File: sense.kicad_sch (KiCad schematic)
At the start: 35 parts, among them J6 Rudder, J7 End Stops, J8 Conn_01x02, J9 ISP, U4 AMS1117-5.0, U6 LM317, U7 ATmega328P-AU, Y1 8mhz

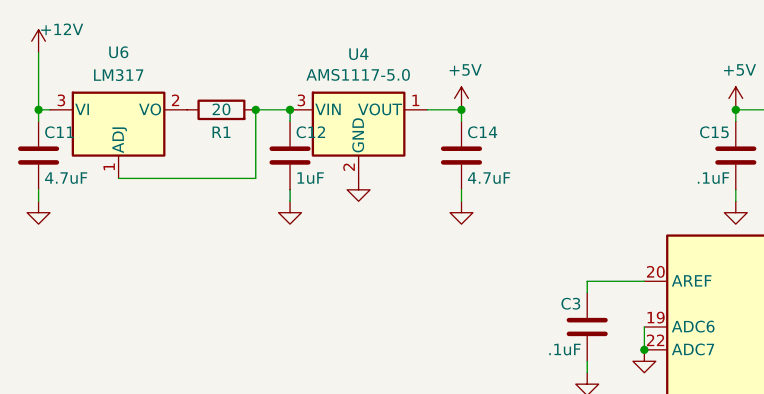
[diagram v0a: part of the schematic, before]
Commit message: Switch from using AMS1117-5.0 to XC6202P502FR-G 5V 200mA LDO regulator
This is what's in the CSV file as the regulator that's being used
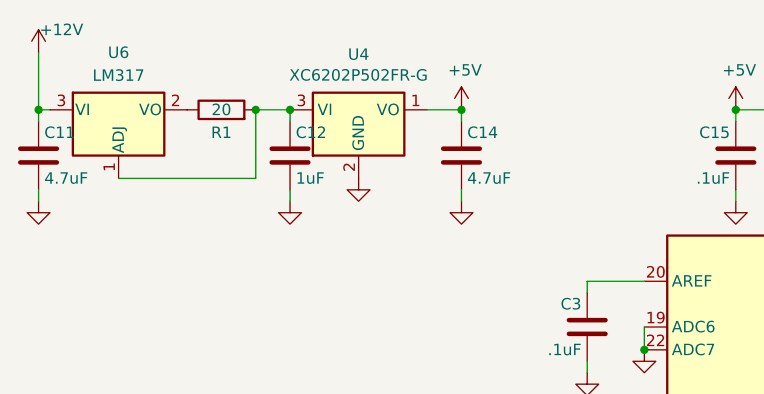
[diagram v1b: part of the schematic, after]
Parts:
- U4: value AMS1117-5.0 -> XC6202P502FR-G; symbol Regulator_Linear:AP2204RB-5.0 -> pypilot_components:XC6202P502FR-G
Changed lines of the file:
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@@
 	)
 	(symbol
-		(lib_id "Regulator_Linear:AP2204RB-5.0")
+		(lib_id "pypilot_components:XC6202P502FR-G")
 		(at 73.66 31.75 0)
 		(unit 1)
@@
 			)
 		)
-		(property "Value" "AMS1117-5.0"
+		(property "Value" "XC6202P502FR-G"
 			(at 73.66 27.9146 0)
 			(effects
@@
 			)
 		)
-		(property "Datasheet" "C513030"
+		(property "Datasheet" "https://www.lcsc.com/datasheet/lcsc_datasheet_2008192005_Torex-Semicon-XC6202P502FR-G_C725695.pdf"
 			(at 76.2 38.1 0)
 			(effects
@@
 			)
 		)
-		(property "Description" ""
+		(property "Description" "200mA Low Dropout regulator, positive, 5.0V fixed output, SOT-223, low power version of AMS1777-5.0"
 			(at 73.66 31.75 0)
 			(effects

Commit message: Remove whitespace from LCSC field entries
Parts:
- C11, C14: LCSC C29823 -> C29823
- LED4: LCSC C2296 -> C2296
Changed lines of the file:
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@@
 			)
 		)
-		(property "LCSC" " C29823"
+		(property "LCSC" "C29823"
 			(at 85.09 36.83 0)
 			(effects
@@
 			)
 		)
-		(property "LCSC" " C29823"
+		(property "LCSC" "C29823"
 			(at 38.1 36.83 0)
 			(effects
@@
 			)
 		)
-		(property "LCSC" " C2296"
+		(property "LCSC" "C2296"
 			(at 97.79 78.74 90)
 			(effects

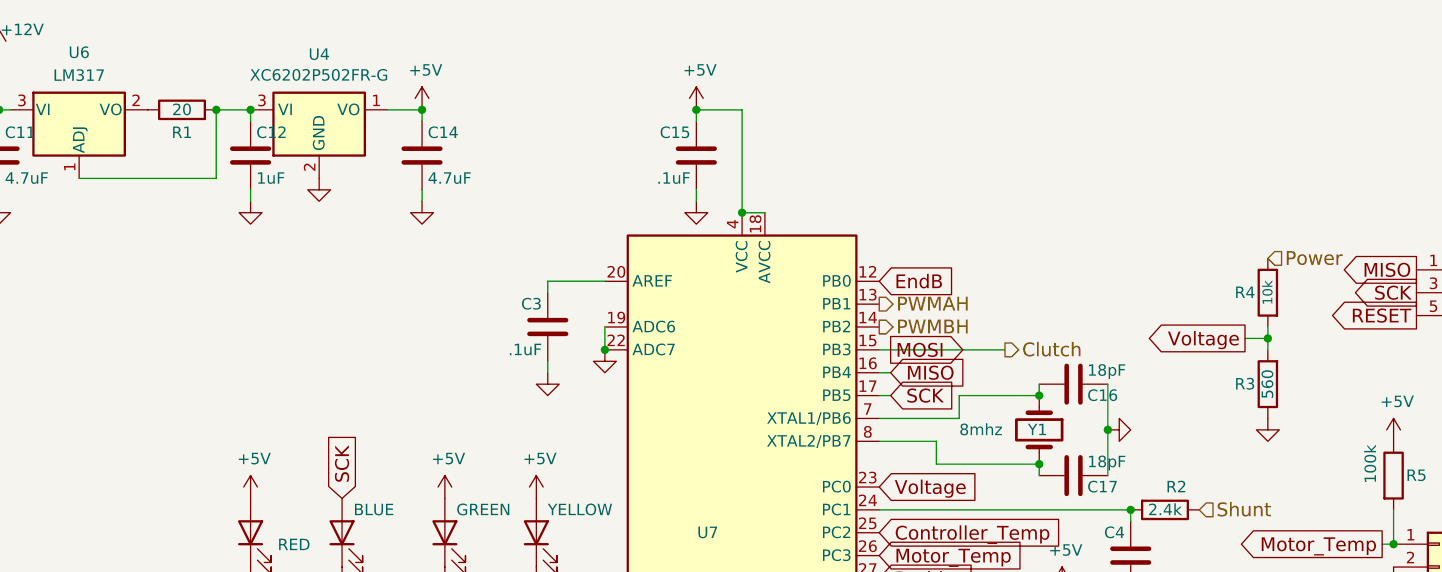
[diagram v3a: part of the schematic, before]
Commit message: Use standard format for resistor values
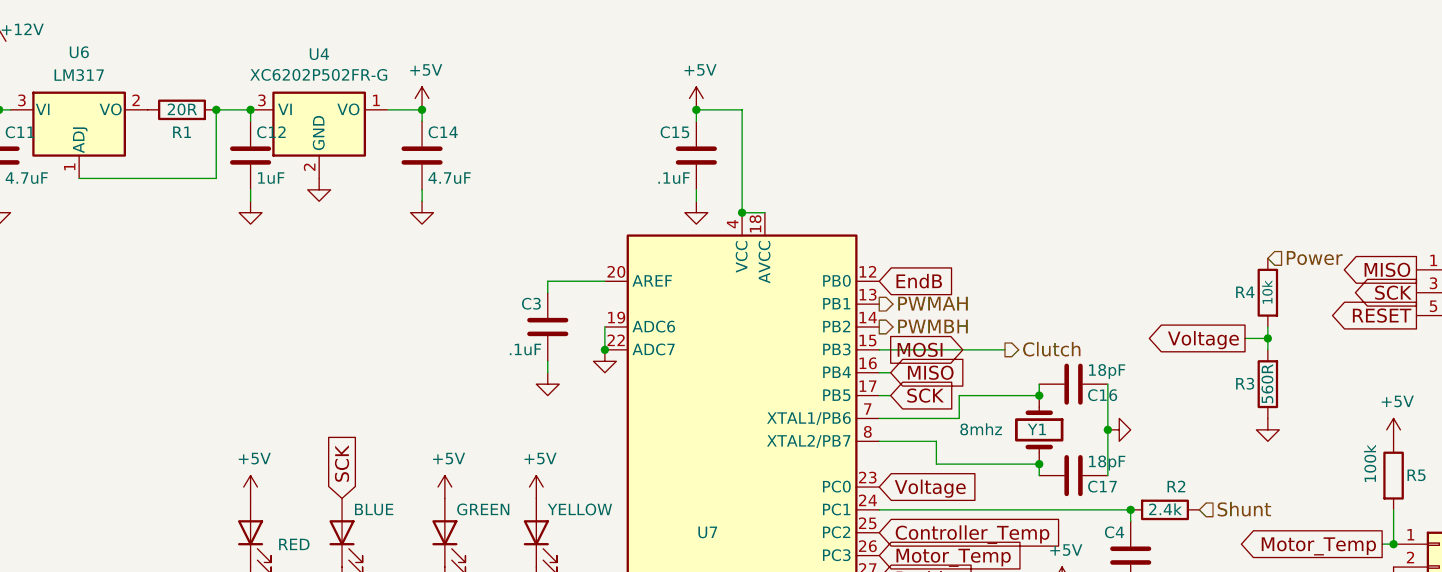
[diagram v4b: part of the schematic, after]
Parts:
- R1: value 20 -> 20R
- R3: value 560 -> 560R
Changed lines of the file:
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@@
 			)
 		)
-		(property "Value" "20"
+		(property "Value" "20R"
 			(at 58.42 31.75 90)
 			(effects
@@
 			)
 		)
-		(property "Value" "560"
+		(property "Value" "560R"
 			(at 179.07 62.23 90)
 			(effects

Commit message: C17 had LCSC part number for 12pF cap, but schematic says 18pF.  Fixed.
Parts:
- C17: LCSC C1792 -> C1797
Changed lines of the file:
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@@
 			)
 		)
-		(property "LCSC" "C1792"
+		(property "LCSC" "C1797"
 			(at 157.48 72.39 90)
 			(effects

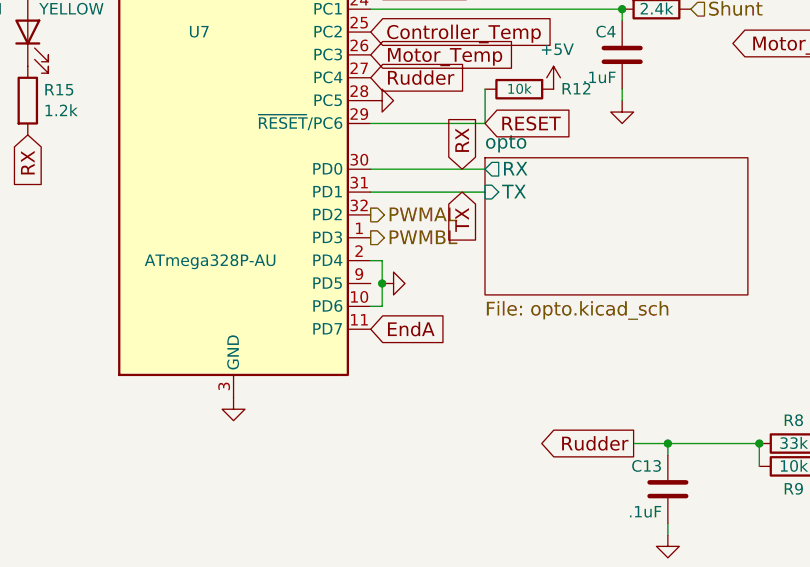
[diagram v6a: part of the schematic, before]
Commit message: Break out PD5, pin 9 of ATmega328
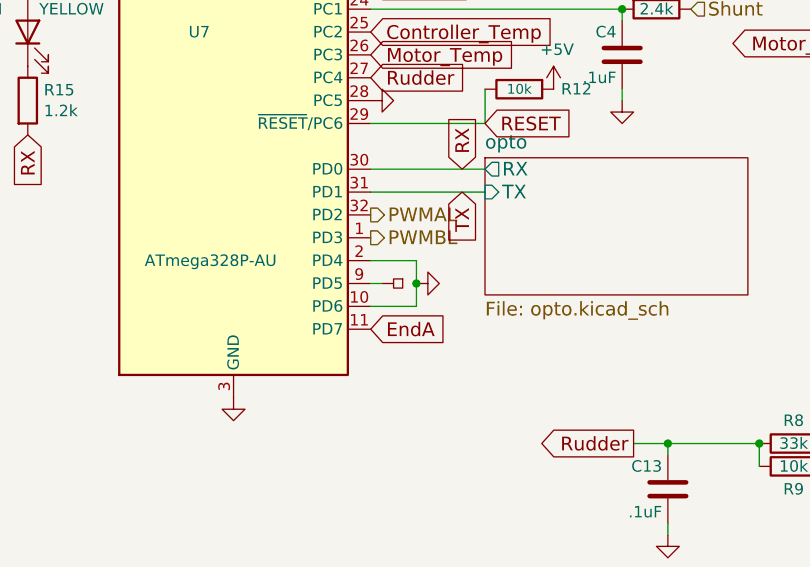
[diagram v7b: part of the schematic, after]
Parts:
- added JP1: PCB_Pin_Breakout, pypilot_controller_footprints:TestPoint_Pad_1.0mm, symbol pypilot_components:PCB_Pin_Breakout
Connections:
- net at U7.9 (PD5): now also JP1.1
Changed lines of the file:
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@@
 	)
 	(junction
-		(at 137.16 106.68)
+		(at 140.97 106.68)
 		(diameter 0)
 		(color 0 0 0 0)
@@
 	(wire
 		(pts
-			(xy 137.16 104.14) (xy 137.16 106.68)
+			(xy 140.97 104.14) (xy 140.97 106.68)
 		)
 		(stroke
@@
 	(wire
 		(pts
+			(xy 135.89 106.68) (xy 137.16 106.68)
+		)
+		(stroke
+			(width 0)
+			(type default)
+		)
+	)
+	(wire
+		(pts
 			(xy 142.24 71.12) (xy 142.24 68.58)
 		)
@@
 	(wire
 		(pts
+			(xy 135.89 109.22) (xy 140.97 109.22)
+		)
+		(stroke
+			(width 0)
+			(type default)
+		)
+	)
+	(wire
+		(pts
 			(xy 191.77 80.01) (xy 193.04 80.01)
 		)
@@
 	(wire
 		(pts
+			(xy 135.89 104.14) (xy 140.97 104.14)
+		)
+		(stroke
+			(width 0)
+			(type default)
+		)
+	)
+	(wire
+		(pts
 			(xy 38.1 31.75) (xy 38.1 25.4)
 		)
@@
 	(wire
 		(pts
-			(xy 135.89 104.14) (xy 137.16 104.14)
-		)
-		(stroke
-			(width 0)
-			(type default)
-		)
-	)
-	(wire
-		(pts
 			(xy 163.83 85.09) (xy 163.83 86.36)
 		)
@@
 	(wire
 		(pts
-			(xy 137.16 106.68) (xy 137.16 109.22)
+			(xy 140.97 106.68) (xy 140.97 109.22)
 		)
 		(stroke
@@
 	(wire
 		(pts
-			(xy 137.16 109.22) (xy 135.89 109.22)
-		)
-		(stroke
-			(width 0)
-			(type default)
-		)
-	)
-	(wire
-		(pts
 			(xy 179.07 57.15) (xy 179.07 58.42)
 		)
@@
 	(symbol
 		(lib_id "power:GND")
-		(at 137.16 106.68 90)
+		(at 140.97 106.68 90)
 		(unit 1)
 		(exclude_from_sim no)
@@
 		(dnp no)
 		(property "Reference" "#PWR0116"
-			(at 143.51 106.68 0)
+			(at 147.32 106.68 0)
 			(effects
 				(font
@@
 		)
 		(property "Value" "GND"
-			(at 140.97 107.95 90)
+			(at 144.78 107.95 90)
 			(effects
 				(font
@@
 		)
 		(property "Footprint" ""
-			(at 137.16 106.68 0)
+			(at 140.97 106.68 0)
 			(effects
 				(font
@@
 		)
 		(property "Datasheet" ""
-			(at 137.16 106.68 0)
+			(at 140.97 106.68 0)
 			(effects
 				(font
@@
 		)
 		(property "Description" "Power symbol creates a global label with name \"GND\" , ground"
-			(at 137.16 106.68 0)
+			(at 140.97 106.68 0)
 			(effects
 				(font
@@
 					(unit 1)
 				)
+			)
+		)
+	)
+	(symbol
+		(lib_id "pypilot_components:PCB_Pin_Breakout")
+		(at 139.7 106.68 0)
+		(unit 1)
+		(exclude_from_sim no)
+		(in_bom no)
+		(on_board yes)
+		(dnp no)
+		(fields_autoplaced yes)
+		(property "Reference" "JP1"
+			(at 139.7 104.648 0)
+			(effects
+				(font
+					(size 1.27 1.27)
+				)
+				(hide yes)
+			)
+		)
+		(property "Value" "PCB_Pin_Breakout"
+			(at 139.954 108.204 0)
+			(effects
+				(font
+					(size 1.27 1.27)
+				)
+				(hide yes)
+			)
+		)
+		(property "Footprint" "pypilot_controller_footprints:TestPoint_Pad_1.0mm"
+			(at 139.7 106.68 0)
+			(effects
+				(font
+					(size 1.27 1.27)
+				)
+				(hide yes)
+			)
+		)
+		(property "Datasheet" "~"
+			(at 139.7 106.68 0)
+			(effects
+				(font
+					(size 1.27 1.27)
+				)
+				(hide yes)
+			)
+		)
+		(property "Description" "PCB pin breakout"
+			(at 139.7 106.68 0)
+			(effects
+				(font
+					(size 1.27 1.27)
+				)
+				(hide yes)
+			)
+		)
+		(pin "1"
+		)
+		(instances
+			(project ""
+				(path "/3485d22d-0932-4f13-a5db-09c3f9bc7038/00000000-0000-0000-0000-000059d8755c"
+					(reference "JP1")
+					(unit 1)
+				)

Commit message: Change TO-252 footprint to use less solder paste
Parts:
- U6: footprint Package_TO_SOT_SMD:TO-252-2 -> pypilot_controller_footprints:TO-252-2-reduced-paste
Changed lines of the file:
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@@
 			)
 		)
-		(property "Footprint" "Package_TO_SOT_SMD:TO-252-2"
+		(property "Footprint" "pypilot_controller_footprints:TO-252-2-reduced-paste"
 			(at 46.99 25.4 0)
 			(effects
